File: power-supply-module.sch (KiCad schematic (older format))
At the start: 69 parts

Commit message: udpate LTC4415 symbol
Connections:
- net 5V_OUT: now also U?.7 (IN2), U?.8 (IN2); no longer U?.6 (~EN2)
- net EN_OUT_A: now also U?.3 (EN1)
- net GND: now also U?.17 (GND)
- net OUT_A_CUR: now also U?.4 (CLIM1)
- net OUT_B_CUR: now also U?.5 (CLIM2)
- net V_OUT_B: now also U?.10 (OUT2), U?.9 (OUT2)
- net ~EN_OUT_B: now also U?.6 (~EN2); no longer U?.3 (EN1)
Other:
- moved on the sheet: R?

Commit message: 1A output limit, OUT A configurable for 2A
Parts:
- added Q?: Q_NMOS_DGS, symbol Q_NMOS_DGS
- added R?: 500, symbol R
- L?: value INDUCTOR -> 3.3uH
- R? (x2): value R -> 500
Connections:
- net GND: now also Q?.3 (S)
- net OUT_A_CUR: now also R?.1
- net OUT_B_WARN: now reaches U?.12 (~WARN2)
- net OUT_A_WARN: now reaches U?.13 (~WARN1)
- new net: Q?.1 (D), R?.2
- new net OUT_A_2AMP: Q?.2 (G)
- no-connect marks 0 -> 2
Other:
- note added: "1000*0.5/1"
- note added: "1A current limit"
- note added: "2A current limit\nfor OUT A"
- note added: "5V, 1A (Vin > 6V) each.\nOUT A can be configured to 2A"
- note removed: "5V, 2A (Vin > 6V)"
- moved on the sheet: C?, D?, U?

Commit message: capacitors & TVS
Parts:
- removed C? (x2): C, symbol C
- removed C?: 0.1uF, symbol C
- removed U?: LTC1844-3.3, MODULE, symbol LTC1844-3.3
- added C? (x2): C, symbol C
- added C?: 1uF, symbol C
- added C?: 47nF, symbol C
- added C?: 10nF, symbol C
- added D? (x2): TVS 5V, symbol ZENERsmall
- added D? (x2): TVS 18V, symbol ZENERsmall
- added R? (x3): 10k, symbol R
- added U?: MCP1703, symbol MCP1703
- C? (x2): value 100uF -> 22uF
- C? (x2): value C -> 0.1uF
- C?: value C -> 22pF
- C?: value C -> 1.8nF
- C?: value C -> 47nF
- C?: value C -> 10nF
- C?: value 4.7u -> 4.7uF
- C?: value 1uF -> 10uF
- R? (x6): value R -> 10k
- R? (x2): value R -> 51k
- R?: value R -> 400k
- R?: value R -> 100k
- R?: value R -> 40.2k
- R? (x2): value R -> 18k
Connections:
- net 5V_OUT: now also R?.1
- net EN_OUT_A: now also R?.1
- net GND: now also C?.2, U?.5 (SHDN), C?.2, C?.2, C?.2, C?.2, D?.2 (A), D?.2 (A), D?.2 (A), D?.2 (A), R?.2, R?.2, U?.1 (GND)
- net MON_V_IN_A: now also C?.1
- net MON_V_IN_B: now also C?.1
- net OUT_A_2AMP: now also R?.1
- net VCC: now also C?.1, U?.2 (OUT)
- net V_IN_A: now also D?.1 (K); no longer C?.2
- net V_IN_B: now also D?.1 (K)
- net V_OUT_A: now also D?.1 (K)
- net V_OUT_B: now also D?.1 (K)
- net ~EN_OUT_B: now also R?.2
- net CAN_TX: now reaches U?.1 (TXD)
- net CAN_RX: now reaches U?.4 (RXD)
- net CAN_STANDBY: now reaches U?.8 (RS)
- net at C?.1, D?.1 (K), D?.1 (K): now also U?.3 (IN)
- net at U?.19 (CP2): now also C?.2
- net at U?.20 (CN2): now also C?.1
- net at U?.21 (CM2): now also C?.1
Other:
- note added: "2x 5V, 1A (Vin > 6V).\nOUT A can be configured to 2A"
- note added: "3.3V"
- note added: "CHECK CURRENT DRAW!!!"
- note added: "M2012LL1W01\nlocking switch"
- note removed: "5V, 1A (Vin > 6V) each.\nOUT A can be configured to 2A"
- moved on the sheet: C?, CONN?, D?, R?

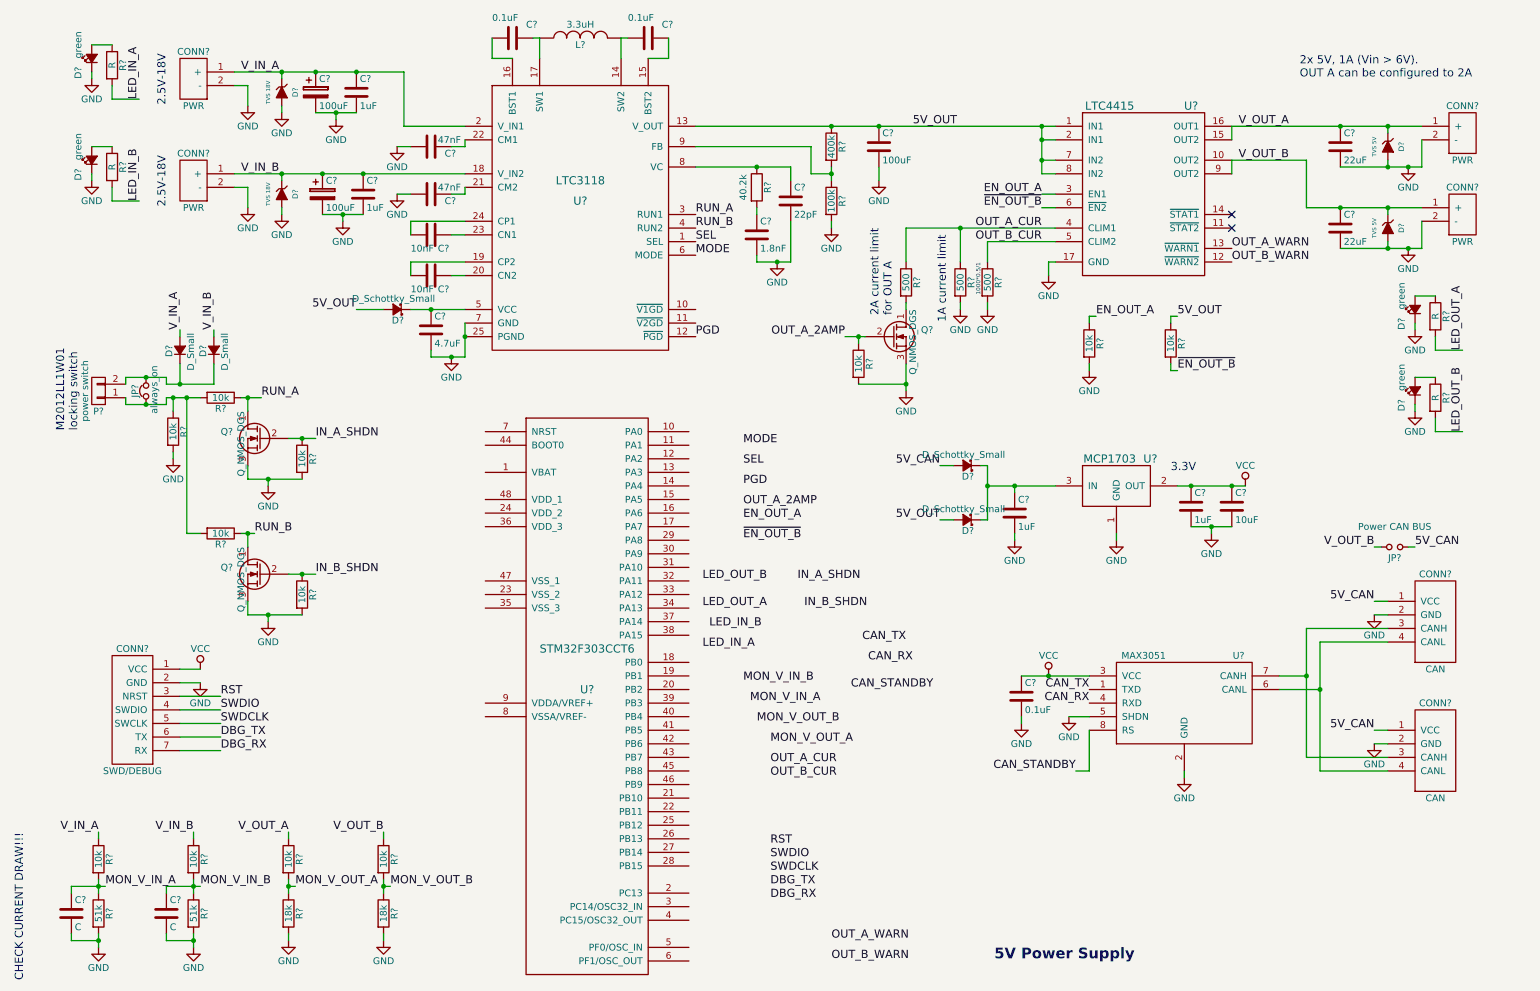
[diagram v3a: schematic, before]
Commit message: diodes & mosfet selection
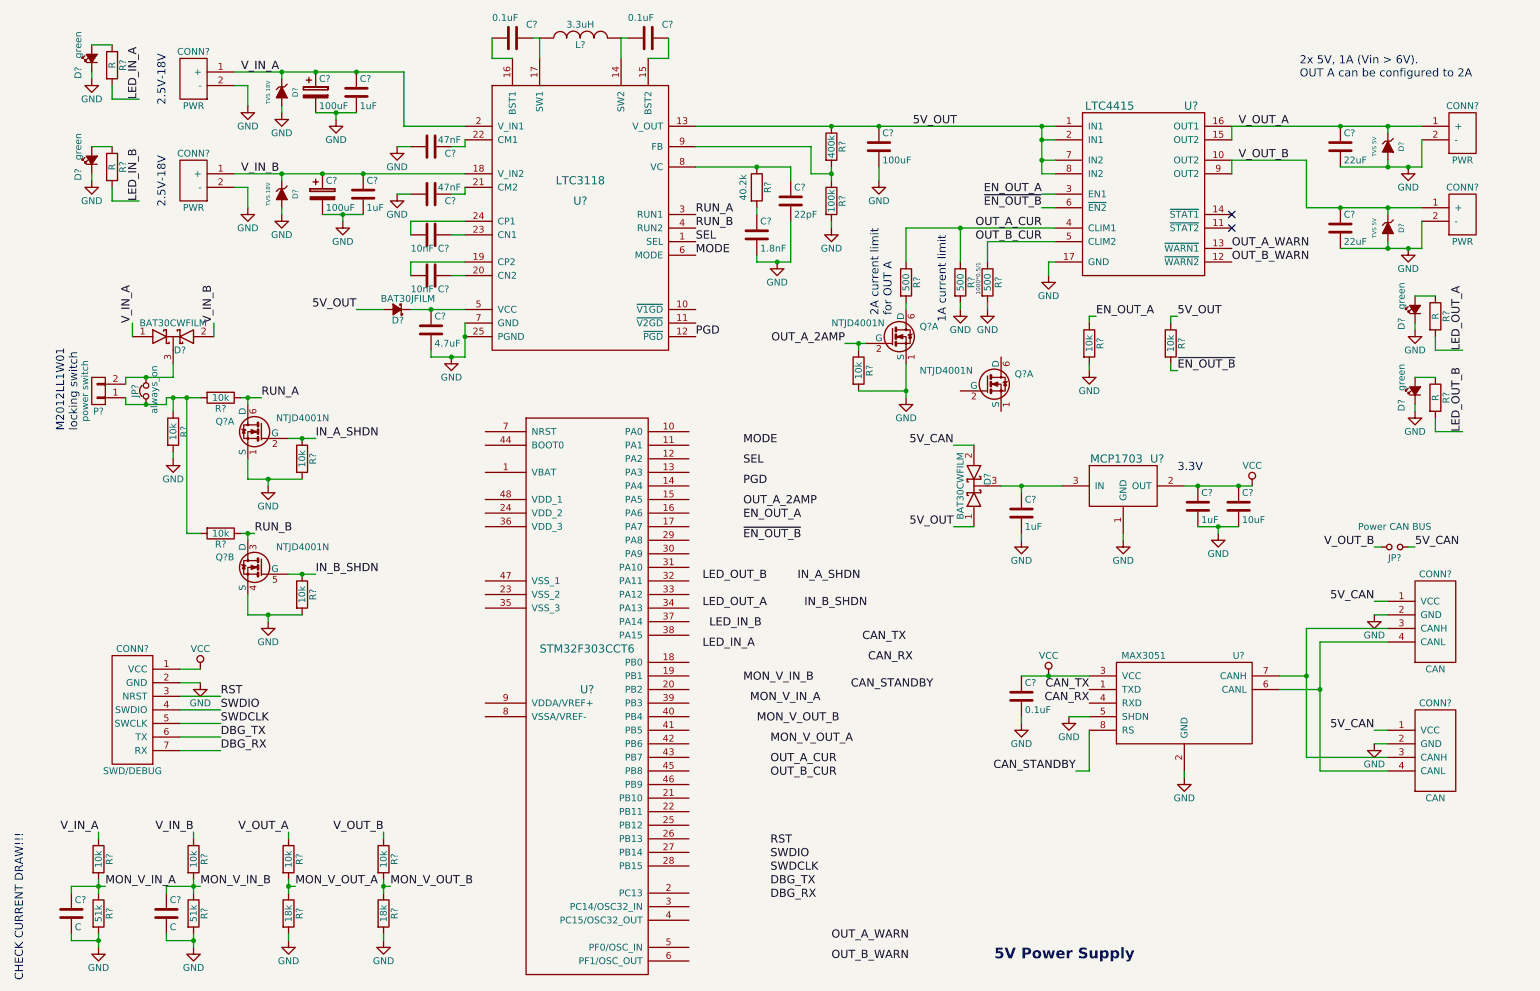
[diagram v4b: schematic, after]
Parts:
- removed D? (x2): D_Schottky_Small, symbol D_Schottky_Small
- removed D? (x2): D_Small, symbol D_Small
- removed Q? (x3): Q_NMOS_DGS, symbol Q_NMOS_DGS
- added D? (x2): BAT30CWFILM, symbol D_Schottky_x2_KCom_AAK
- added Q? (x4): NTJD4001N, SC-70-6, symbol NTJD4001N
- D?: value D_Schottky_Small -> BAT30JFILM
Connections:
- net 5V_CAN: now also D?.2 (A)
- net 5V_OUT: now also D?.1 (A)
- net GND: now also Q?.1 (S), Q?.1 (S), Q?.4 (S)
- net IN_A_SHDN: now also Q?.2 (G)
- net IN_B_SHDN: now also Q?.5 (G)
- net OUT_A_2AMP: now also Q?.2 (G)
- net RUN_A: now also Q?.6 (D)
- net RUN_B: now also Q?.3 (D)
- net V_IN_A: now also D?.1 (A)
- net V_IN_B: now also D?.2 (A)
- net at C?.1, U?.3 (IN): now also D?.3 (K)
- net at JP?.2, P?.2 (P2): now also D?.3 (K)
- net at R?.2: now also Q?.6 (D)
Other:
- moved on the sheet: C?, R?, U?
